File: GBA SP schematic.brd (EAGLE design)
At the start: 100.5 x 100 mm, 187 parts, among them IC2 FT230XQ, J1 DNP, J11 Debug USB, J12 FPC_14, J13 DNP, J14 FPC_14, J2 MICRO_USB, J4 DNP, J5 DNP, J6 FPC_14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

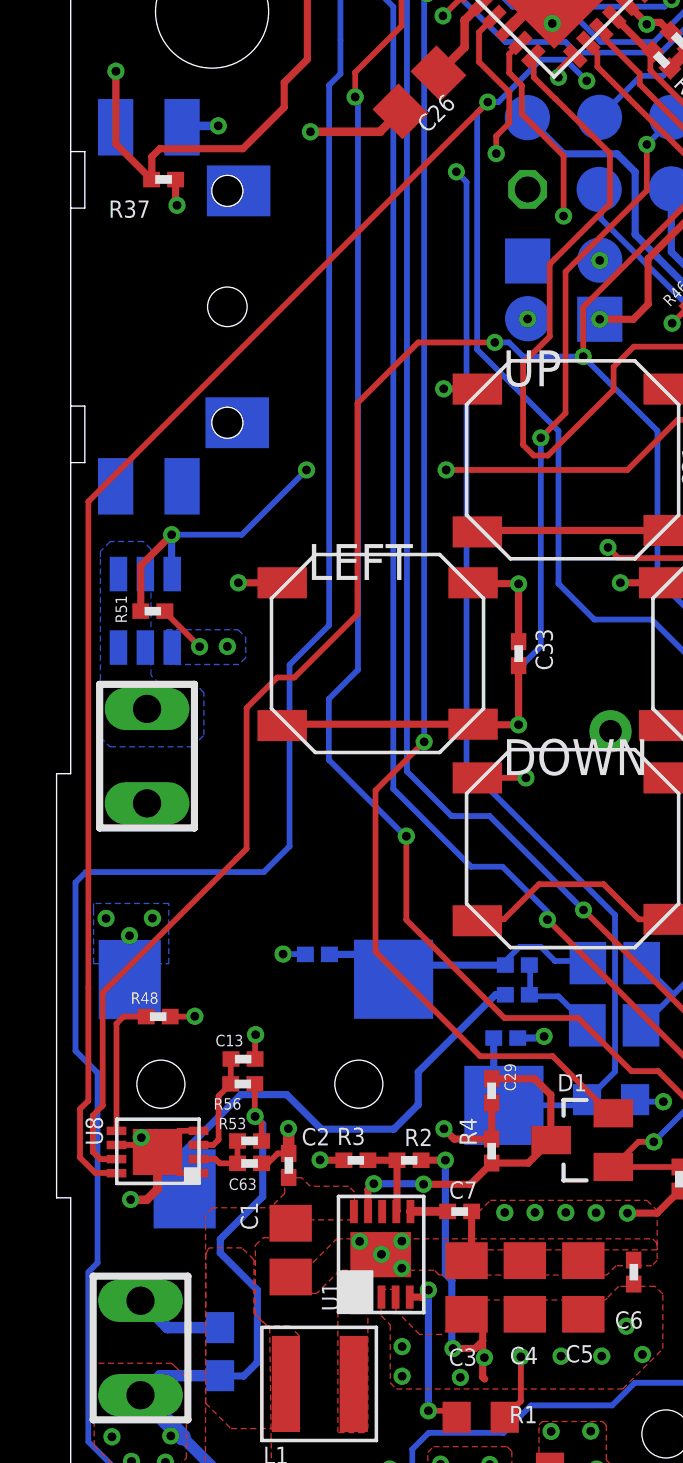
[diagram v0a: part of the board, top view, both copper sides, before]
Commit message: Pull-up for battery monitor
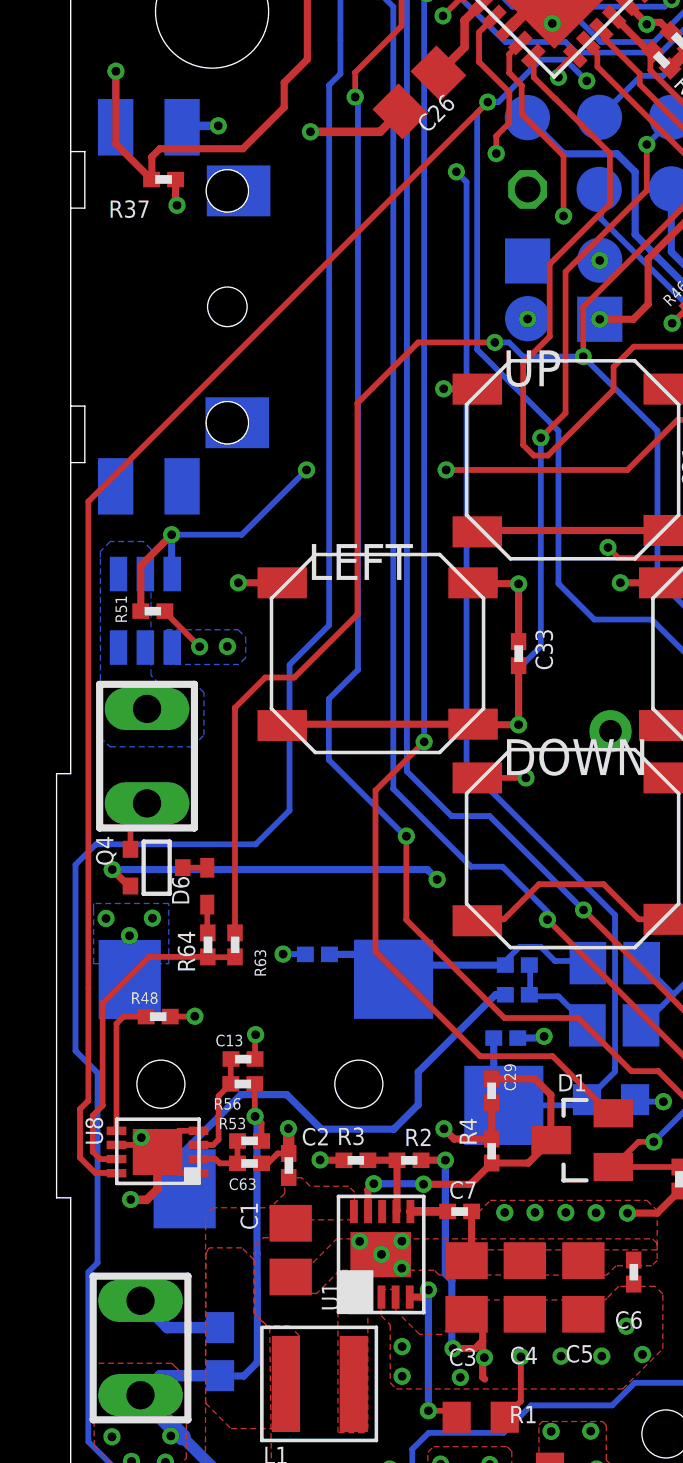
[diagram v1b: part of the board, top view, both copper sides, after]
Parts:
- added D6: (no value), diode:SOD523
- added Q4: PMOS, Custom_Library:SC70
- added R63: 1k, rcl:0402_REAL
- added R64: 499, rcl:0402_REAL
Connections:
- new net N$32: D6.C, R64.2
- new net N$40: D6.A, Q4.D
- new net N$99: R63.1, R64.1, U8.7
- net 5V: now also Q4.G
- net PWR_IN: now also Q4.S
- net SCL: now also R63.2; no longer U8.7
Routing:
- net PWR_IN: track 197.0 -> 222.2 mm, vias 18 -> 20
- net N$99: track 0.00 -> 11.7 mm
- net SCL: track 113.1 -> 102.6 mm
- net 5V: track 49.3 -> 51.2 mm
- net V_BAT: track 36.4 -> 35.2 mm
- net N$32: track 0.00 -> 1.01 mm
- net N$40: track 0.00 -> 0.87 mm
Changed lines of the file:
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@@
 <layers>
 <layer number="1" name="Top" color="4" fill="1" visible="yes" active="yes"/>
-<layer number="2" name="Route2" color="1" fill="3" visible="yes" active="yes"/>
+<layer number="2" name="Route2" color="1" fill="3" visible="no" active="yes"/>
 <layer number="3" name="Route3" color="4" fill="3" visible="no" active="no"/>
 <layer number="4" name="Route4" color="1" fill="4" visible="no" active="no"/>
@@
 <layer number="13" name="Route13" color="4" fill="5" visible="no" active="no"/>
 <layer number="14" name="Route14" color="1" fill="6" visible="no" active="no"/>
-<layer number="15" name="Route15" color="25" fill="6" visible="yes" active="yes"/>
+<layer number="15" name="Route15" color="25" fill="6" visible="no" active="yes"/>
 <layer number="16" name="Bottom" color="1" fill="1" visible="yes" active="yes"/>
 <layer number="17" name="Pads" color="2" fill="1" visible="yes" active="yes"/>
@@
 <attribute name="MPN" value="CSS-1210TB" x="73.73" y="22.54" size="1.778" layer="28" rot="MR270" display="off"/>
 </element>
+<element name="R63" library="rcl" package="0402_REAL" value="1k" x="5.8205" y="31.95150625" smashed="yes" rot="R90">
+<attribute name="NAME" x="6.9105" y="30.81150625" size="0.4064" layer="25" rot="R90"/>
+<attribute name="VALUE" x="6.6705" y="30.78150625" size="0.4064" layer="27" rot="R90"/>
+</element>
+<element name="Q4" library="Custom_Library" package="SC70" value="PMOS" x="3.04020625" y="34.67565" smashed="yes" rot="R270">
+<attribute name="NAME" x="1.50979375" y="34.73435" size="0.6096" layer="25" rot="R90"/>
+<attribute name="VALUE" x="0.44020625" y="35.67565" size="1.27" layer="27" rot="R270"/>
+</element>
+<element name="D6" library="diode" package="SOD523" value="" x="4.83" y="33.97" smashed="yes" rot="R90">
+<attribute name="NAME" x="4.195" y="33.335" size="0.6096" layer="25" rot="R90"/>
+<attribute name="VALUE" x="6.735" y="33.335" size="1.27" layer="27" rot="R90"/>
+</element>
+<element name="R64" library="rcl" package="0402_REAL" value="499" x="4.86" y="31.95" smashed="yes" rot="R90">
+<attribute name="NAME" x="4.4" y="30.97" size="0.6096" layer="25" rot="R90"/>
+<attribute name="VALUE" x="5.71" y="30.78" size="0.4064" layer="27" rot="R90"/>
+</element>
 </elements>
 <signals>
@@
 <wire x1="3.71" y1="59.01" x2="3.71" y2="58.15" width="0.254" layer="1"/>
 <wire x1="3.71" y1="58.15" x2="3.76" y2="58.1" width="0.254" layer="1"/>
+<contactref element="Q4" pad="G"/>
+<wire x1="2.11520625" y1="35.32565" x2="2.11520625" y2="36.36520625" width="0.205" layer="1"/>
+<wire x1="2.11520625" y1="36.36520625" x2="2.7" y2="36.95" width="0.205" layer="1"/>
 </signal>
 <signal name="N$3">
@@
 <wire x1="27.69" y1="73.65" x2="27.69" y2="71.19" width="0.4064" layer="1"/>
 <wire x1="27.69" y1="71.19" x2="28.32" y2="70.56" width="0.4064" layer="1"/>
+<contactref element="Q4" pad="S"/>
+<wire x1="2.11520625" y1="34.02565" x2="2.05435" y2="34.02565" width="0.254" layer="1"/>
+<wire x1="2.05435" y1="34.02565" x2="1.47" y2="34.61" width="0.254" layer="1"/>
+<via x="1.47" y="34.61" extent="1-16" drill="0.31"/>
+<wire x1="1.47" y1="34.61" x2="12.61" y2="34.61" width="0.254" layer="16"/>
+<wire x1="12.61" y1="34.61" x2="12.96" y2="34.26" width="0.254" layer="16"/>
+<via x="12.96" y="34.26" extent="1-16" drill="0.31"/>
+<wire x1="12.96" y1="34.26" x2="19.32" y2="34.26" width="0.254" layer="15"/>
+<wire x1="19.32" y1="34.26" x2="23.82" y2="29.76" width="0.254" layer="15"/>
 </signal>
 <signal name="V_BAT">
@@
 <wire x1="2.83" y1="15.66" x2="2.47" y2="16.02" width="0.4064" layer="16"/>
 <wire x1="3.95" y1="14.54" x2="2.83" y2="15.66" width="0.6" layer="16"/>
-<wire x1="5.29" y1="21.05" x2="6.6" y2="19.74" width="0.254" layer="16"/>
+<wire x1="6.59" y1="21.03" x2="6.6" y2="19.74" width="0.254" layer="16"/>
 <wire x1="6.6" y1="19.74" x2="6.6" y2="17.18" width="0.254" layer="16"/>
 <wire x1="6.6" y1="17.18" x2="6.12" y2="16.7" width="0.254" layer="16"/>
@@
 <wire x1="5.29" y1="16.7" x2="5.28" y2="16.71" width="0.254" layer="16"/>
 <via x="6.52" y="25.88" extent="1-16" drill="0.31"/>
-<wire x1="6.52" y1="25.88" x2="6.79" y2="25.61" width="0.254" layer="16"/>
-<wire x1="6.79" y1="25.61" x2="6.79" y2="23.04" width="0.254" layer="16"/>
-<wire x1="6.79" y1="23.04" x2="5.29" y2="21.54" width="0.254" layer="16"/>
-<wire x1="5.29" y1="21.54" x2="5.29" y2="21.05" width="0.254" layer="16"/>
 <contactref element="D2" pad="1"/>
 <wire x1="9.24" y1="11.11" x2="8.325" y2="10.195" width="0.3048" layer="16"/>
@@
 <wire x1="6.51" y1="27.03" x2="6.51" y2="25.89" width="0.205" layer="1"/>
 <wire x1="6.51" y1="25.89" x2="6.52" y2="25.88" width="0.205" layer="1"/>
+<wire x1="6.59" y1="21.03" x2="6.59" y2="25.81" width="0.254" layer="16"/>
+<wire x1="6.59" y1="25.81" x2="6.52" y2="25.88" width="0.254" layer="16"/>
 </signal>
 <signal name="N$5">
@@
 <wire x1="19.2227375" y1="64.76098125" x2="20.444103125" y2="63.539615625" width="0.254" layer="1"/>
 <wire x1="20.444103125" y1="63.539615625" x2="20.590084375" y2="63.539615625" width="0.254" layer="1"/>
-<wire x1="5.875" y1="35" x2="1.625" y2="30.75" width="0.2032" layer="1"/>
 <wire x1="15" y1="53.25" x2="14.125" y2="53.25" width="0.2032" layer="1"/>
 <wire x1="15.5" y1="53.25" x2="15" y2="53.25" width="0.2032" layer="16"/>
@@
 <wire x1="10.14" y1="51.1" x2="10.14" y2="43.63" width="0.205" layer="1"/>
 <wire x1="10.14" y1="43.63" x2="7.91" y2="41.4" width="0.205" layer="1"/>
-<wire x1="7.91" y1="41.4" x2="7.3" y2="41.4" width="0.205" layer="1"/>
-<wire x1="7.3" y1="41.4" x2="6.22" y2="40.32" width="0.205" layer="1"/>
-<wire x1="6.22" y1="40.32" x2="6.22" y2="35.345" width="0.205" layer="1"/>
-<wire x1="6.22" y1="35.345" x2="5.875" y2="35" width="0.205" layer="1"/>
-<contactref element="U8" pad="7"/>
-<wire x1="1.625" y1="30.75" x2="1.13" y2="30.255" width="0.205" layer="1"/>
-<wire x1="1.13" y1="30.255" x2="1.13" y2="26.26" width="0.205" layer="1"/>
-<wire x1="1.13" y1="26.26" x2="0.78" y2="25.91" width="0.205" layer="1"/>
-<wire x1="0.78" y1="25.91" x2="0.78" y2="24.63" width="0.205" layer="1"/>
-<wire x1="0.78" y1="24.63" x2="1.04" y2="24.37" width="0.205" layer="1"/>
-<wire x1="1.04" y1="24.37" x2="1.62" y2="24.37" width="0.205" layer="1"/>
+<wire x1="7.91" y1="41.4" x2="6.88" y2="41.4" width="0.205" layer="1"/>
 <wire x1="50.375" y1="26" x2="50.8" y2="25.575" width="0.205" layer="16"/>
 <wire x1="50.8" y1="25.575" x2="50.8" y2="24.63" width="0.205" layer="16"/>
@@
 <wire x1="55.93" y1="23.24" x2="57.365" y2="23.24" width="0.205" layer="16"/>
 <wire x1="57.365" y1="23.24" x2="57.375" y2="23.25" width="0.205" layer="16"/>
+<contactref element="R63" pad="2"/>
+<wire x1="5.8105" y1="32.37150625" x2="5.8105" y2="40.3305" width="0.205" layer="1"/>
+<wire x1="5.8105" y1="40.3305" x2="6.88" y2="41.4" width="0.205" layer="1"/>
 </signal>
 <signal name="MICRO_5V">
@@
 <contactref element="C59" pad="1"/>
 <wire x1="9.54" y1="65.67" x2="8.62" y2="65.67" width="0.205" layer="16"/>
-<wire x1="7.74" y1="41.85" x2="7.74" y2="35.43" width="0.205" layer="16"/>
-<wire x1="7.74" y1="35.43" x2="6.83" y2="34.52" width="0.205" layer="16"/>
-<wire x1="6.83" y1="34.52" x2="0.54" y2="34.52" width="0.205" layer="16"/>
-<wire x1="0.54" y1="34.52" x2="0.17" y2="34.15" width="0.205" layer="16"/>
-<wire x1="0.17" y1="34.15" x2="0.17" y2="28.2" width="0.205" layer="16"/>
+<wire x1="7.74" y1="41.85" x2="7.74" y2="36.7" width="0.205" layer="16"/>
+<wire x1="0.17" y1="34.78" x2="0.17" y2="28.2" width="0.205" layer="16"/>
 <wire x1="0.17" y1="28.2" x2="0.95" y2="27.42" width="0.205" layer="16"/>
 <wire x1="0.95" y1="27.42" x2="0.95" y2="20.7" width="0.205" layer="16"/>
@@
 <wire x1="56.65" y1="10.5" x2="57.77" y2="9.38" width="0.205" layer="1"/>
 <wire x1="57.77" y1="9.38" x2="57.77" y2="8.12" width="0.205" layer="1"/>
+<wire x1="0.17" y1="34.78" x2="0.89" y2="35.5" width="0.205" layer="16"/>
+<wire x1="0.89" y1="35.5" x2="6.54" y2="35.5" width="0.205" layer="16"/>
+<wire x1="6.54" y1="35.5" x2="7.74" y2="36.7" width="0.205" layer="16"/>
 </signal>
 <signal name="PGD">
@@
 <wire x1="1.87" y1="29.41" x2="2.67" y2="29.41" width="0.205" layer="1"/>
 </signal>
+<signal name="N$99">
+<contactref element="U8" pad="7"/>
+<contactref element="R63" pad="1"/>
+<wire x1="1.13" y1="29.88" x2="1.13" y2="26.26" width="0.205" layer="1"/>
+<wire x1="1.13" y1="26.26" x2="0.78" y2="25.91" width="0.205" layer="1"/>
+<wire x1="0.78" y1="25.91" x2="0.78" y2="24.63" width="0.205" layer="1"/>
+<wire x1="0.78" y1="24.63" x2="1.04" y2="24.37" width="0.205" layer="1"/>
+<wire x1="1.04" y1="24.37" x2="1.62" y2="24.37" width="0.205" layer="1"/>
+<contactref element="R64" pad="1"/>
+<wire x1="4.86" y1="31.51" x2="4.85" y2="31.52" width="0.205" layer="1"/>
+<wire x1="4.85" y1="31.52" x2="2.77" y2="31.52" width="0.205" layer="1"/>
+<wire x1="2.77" y1="31.52" x2="1.13" y2="29.88" width="0.205" layer="1"/>
+<wire x1="4.86" y1="31.51" x2="5.79899375" y2="31.51" width="0.205" layer="1"/>
+<wire x1="5.79899375" y1="31.51" x2="5.8105" y2="31.52150625" width="0.205" layer="1"/>
+</signal>
+<signal name="N$32">
+<contactref element="R64" pad="2"/>
+<contactref element="D6" pad="C"/>
+<wire x1="4.83" y1="33.37" x2="4.83" y2="32.39" width="0.205" layer="1"/>
+<wire x1="4.83" y1="32.39" x2="4.85" y2="32.37" width="0.205" layer="1"/>
+</signal>
+<signal name="N$40">
+<contactref element="D6" pad="A"/>
+<contactref element="Q4" pad="D"/>
+<wire x1="3.96520625" y1="34.67565" x2="4.82435" y2="34.67565" width="0.205" layer="1"/>
+<wire x1="4.82435" y1="34.67565" x2="4.83" y2="34.67" width="0.205" layer="1"/>
+</signal>
 </signals>
